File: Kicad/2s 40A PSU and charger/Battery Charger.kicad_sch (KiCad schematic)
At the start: 42 parts

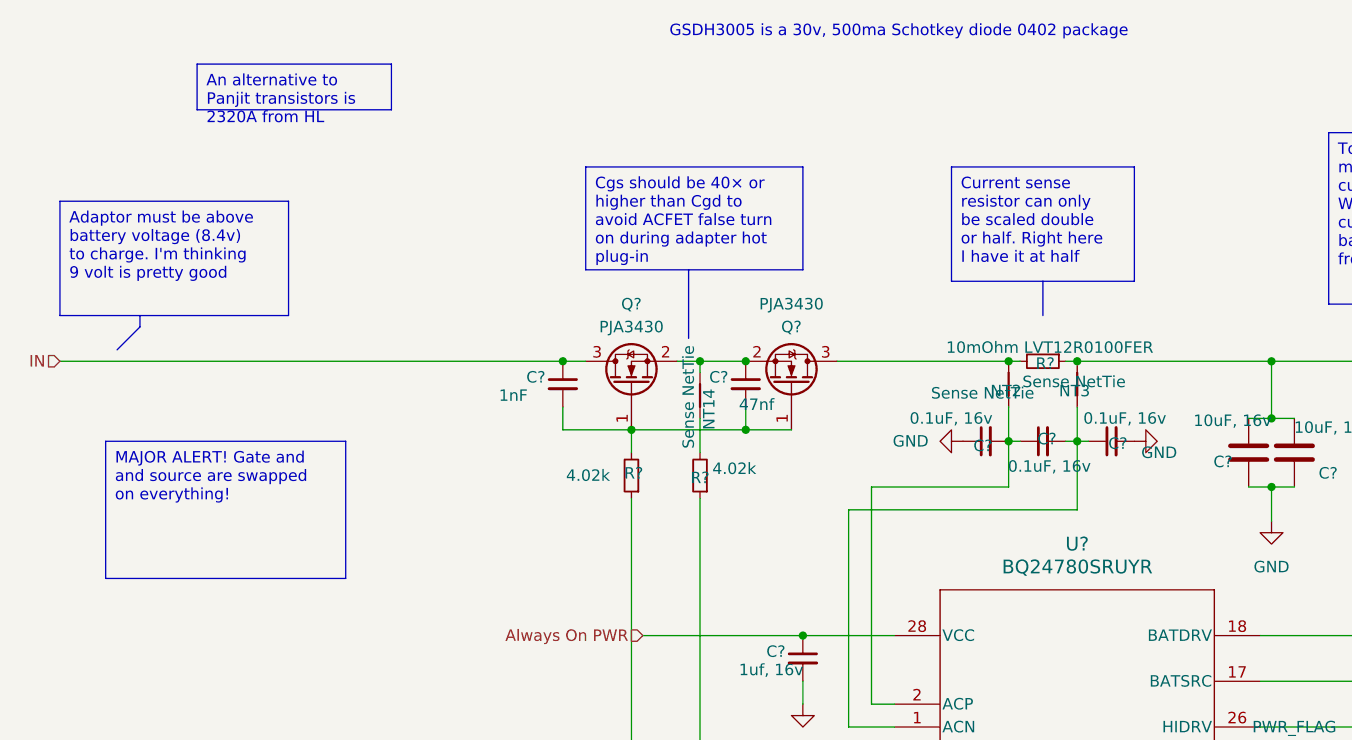
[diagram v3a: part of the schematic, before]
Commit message: Final tweaks, capacitor placement and GND keepouts
I tried my best to isolate signal grounds from the power paths. I also added a bunch of ground keepouts to help isolate.
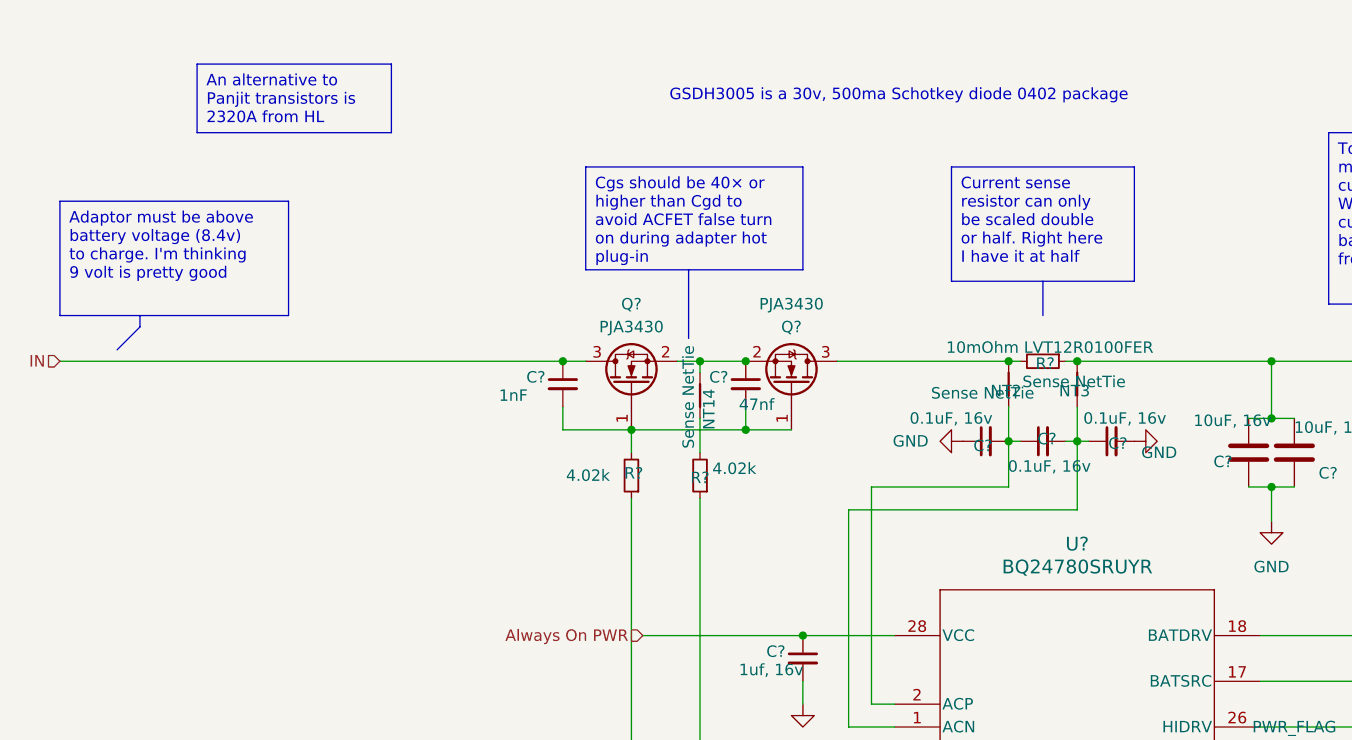
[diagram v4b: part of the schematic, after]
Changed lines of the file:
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@@
 	(title_block
 		(title "CACKLE 2s 40A PSU & Charger")
-		(date "2024-12-01")
+		(date "2024-12-23")
 		(rev "V1")
 		(comment 1 "Author: Asher Edwards")
@@
 		)
 	)
-	(text_box "MAJOR ALERT! Gate and and source are swapped on everything!"
+	(text_box "REGN is a 6v 100ma/13ma output"
 		(exclude_from_sim no)
-		(at 24.13 63.5 0)
-		(size 26.67 15.24)
+		(at 176.53 148.59 0)
+		(size 12.7 10.16)
 		(stroke
 			(width 0)
@@
 		)
 	)
-	(text_box "REGN is a 6v 100ma/13ma output"
+	(text_box "An alternative to Panjit transistors is 2320A from HL"
 		(exclude_from_sim no)
-		(at 176.53 148.59 0)
-		(size 12.7 10.16)
+		(at 34.29 21.59 0)
+		(size 21.59 7.62)
 		(stroke
 			(width 0)
@@
 		)
 	)
-	(text_box "An alternative to Panjit transistors is 2320A from HL"
+	(text_box "- ProcHot indicates system limit failure\n- PMON is total system power scaled down, so it needs an ext res\n- IDAP and IDCHG indicates adaptor and discharge current w/ Voltage\n- Acok is adaptor present indicator\n- TB_Stat indicated hybrid boost mode\n\nILIM and ACOK should not be left floating "
 		(exclude_from_sim no)
-		(at 34.29 21.59 0)
-		(size 21.59 5.08)
+		(at 25.4 123.19 0)
+		(size 36.83 33.02)
 		(stroke
 			(width 0)
@@
 		)
 	)
-	(text_box "- ProcHot indicates system limit failure\n- PMON is total system power scaled down, so it needs an ext res\n- IDAP and IDCHG indicates adaptor and discharge current w/ Voltage\n- Acok is adaptor present indicator\n- TB_Stat indicated hybrid boost mode\n\nILIM and ACOK should not be left floating "
+	(text "GSDH3005 is a 30v, 500ma Schotkey diode 0402 package"
 		(exclude_from_sim no)
-		(at 25.4 123.19 0)
-		(size 36.83 33.02)
-		(stroke
-			(width 0)
-			(type default)
-		)
-		(fill
-			(type none)
-		)
+		(at 112.268 25.146 0)
 		(effects
 			(font
-				(size 1.27 1.27)
-			)
-			(justify left top)
-		)
-	)
-	(text "GSDH3005 is a 30v, 500ma Schotkey diode 0402 package"
-		(exclude_from_sim no)
-		(at 112.268 18.034 0)
-		(effects
-			(font

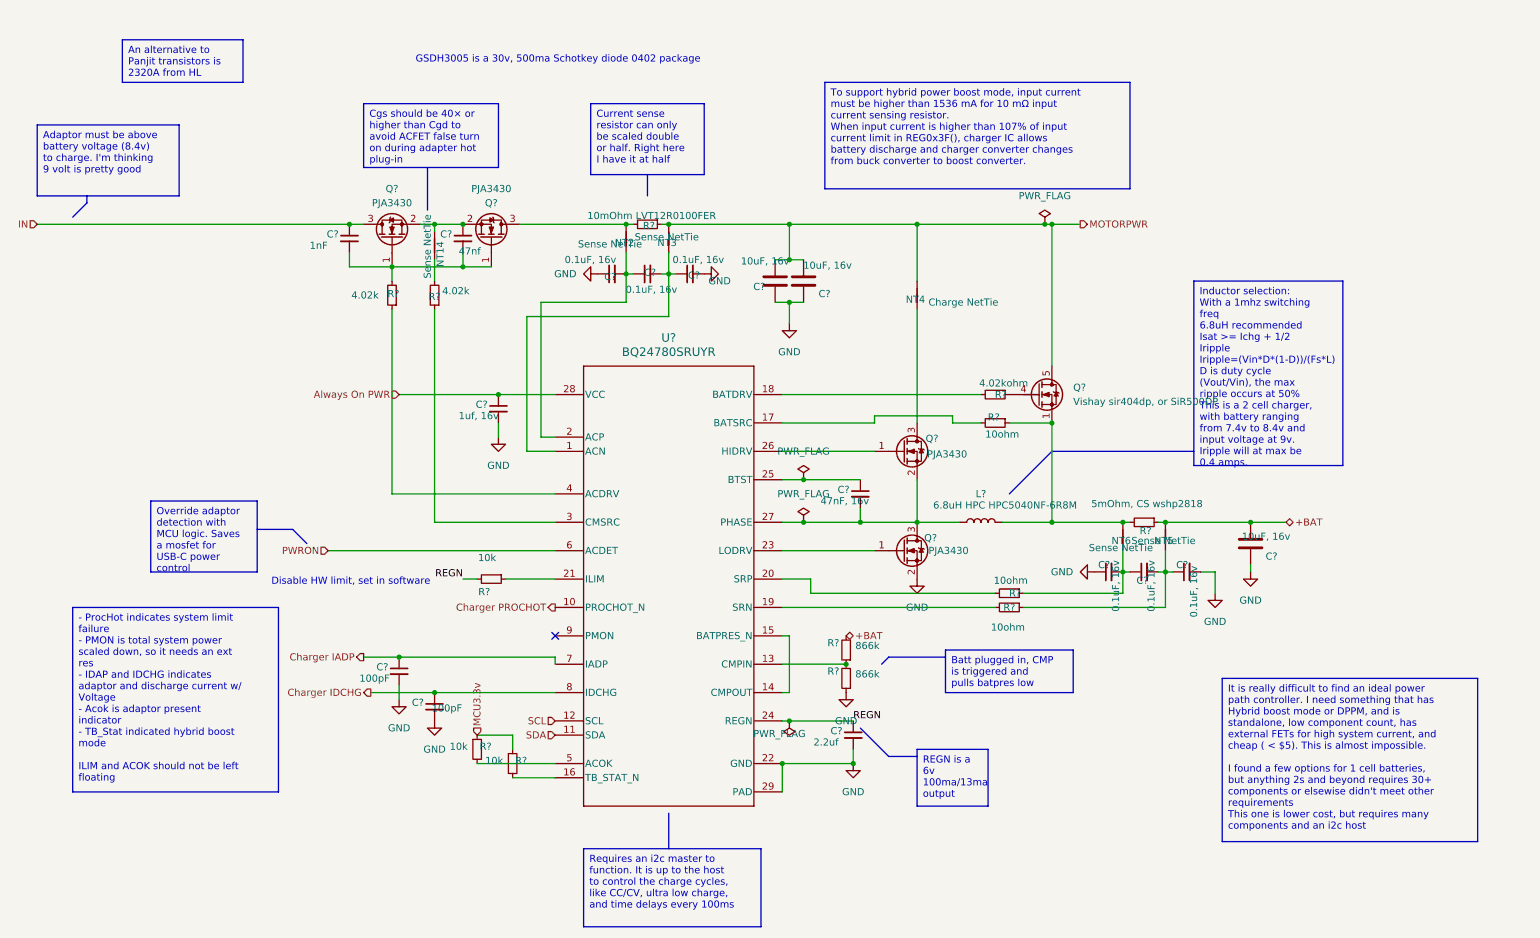
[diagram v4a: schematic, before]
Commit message: Added LCSC part numbers, DNP attr, and exported Gerbers
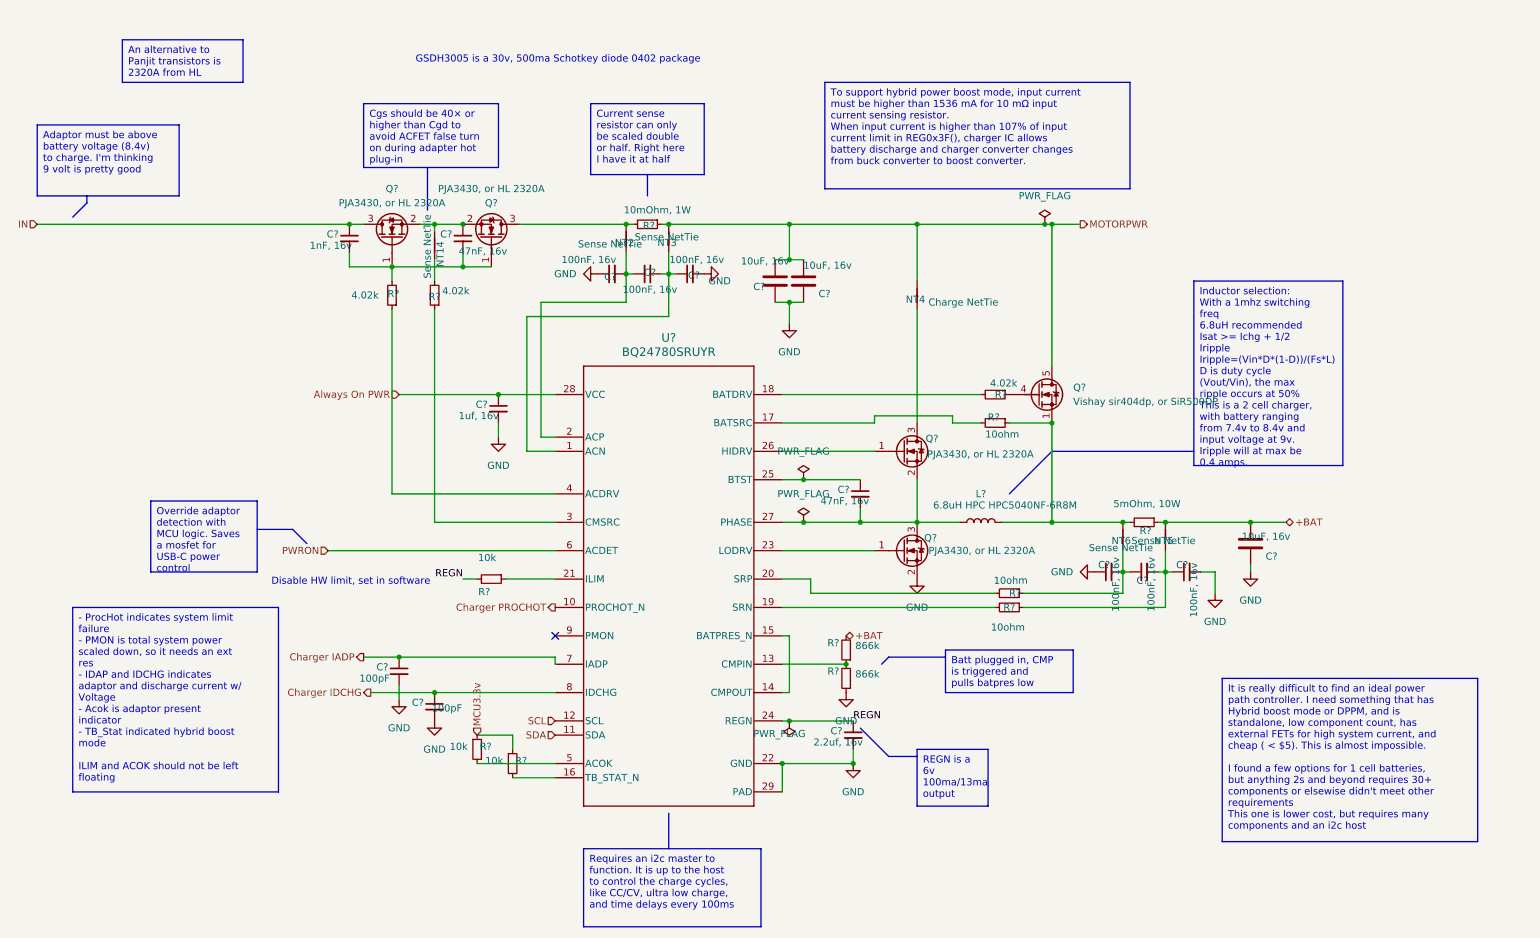
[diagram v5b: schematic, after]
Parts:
- C?: value 47nf -> 47nF, 16v
- C? (x6): value 0.1uF, 16v -> 100nF, 16v
- C?: value 1nF -> 1nF, 16v
- C?: value 2.2uf -> 2.2uf, 16v
- Q? (x4): value PJA3430 -> PJA3430, or HL 2320A
- R?: value 5mOhm, CS wshp2818 -> 5mOhm, 10W
- R?: value 4.02kohm -> 4.02k
- R?: value 10mOhm LVT12R0100FER -> 10mOhm, 1W
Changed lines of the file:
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@@
 			)
 		)
-		(property "Value" "PJA3430"
+		(property "Value" "PJA3430, or HL 2320A"
 			(at 178.562 113.03 0)
 			(effects
@@
 			)
 		)
-		(property "Value" "47nf"
+		(property "Value" "47nF, 16v"
 			(at 94.488 59.436 0)
 			(effects
@@
 			)
 		)
-		(property "Value" "5mOhm, CS wshp2818"
+		(property "Value" "5mOhm, 10W"
 			(at 217.678 104.648 90)
 			(effects
@@
 			)
 		)
-		(property "Value" "0.1uF, 16v"
+		(property "Value" "100nF, 16v"
 			(at 226.06 124.968 0)
 			(effects
@@
 			)
 		)
-		(property "Value" "0.1uF, 16v"
+		(property "Value" "100nF, 16v"
 			(at 218.44 123.952 0)
 			(effects
@@
 			)
 		)
-		(property "Value" "0.1uF, 16v"
+		(property "Value" "100nF, 16v"
 			(at 133.604 66.294 90)
 			(effects
@@
 			)
 		)
-		(property "Value" "4.02kohm"
+		(property "Value" "4.02k"
 			(at 192.024 83.058 90)
 			(effects
@@
 			)
 		)
-		(property "Value" "0.1uF, 16v"
+		(property "Value" "100nF, 16v"
 			(at 141.986 60.96 90)
 			(effects
@@
 			)
 		)
-		(property "Value" "0.1uF, 16v"
+		(property "Value" "100nF, 16v"
 			(at 122.682 60.96 90)
 			(effects
@@
 			)
 		)
-		(property "Value" "10mOhm LVT12R0100FER"
-			(at 129.032 53.086 90)
+		(property "Value" "10mOhm, 1W"
+			(at 130.048 52.07 90)
 			(effects
 				(font
@@
 			)
 		)
-		(property "Value" "PJA3430"
+		(property "Value" "PJA3430, or HL 2320A"
 			(at 178.308 95.758 0)
 			(effects
@@
 			)
 		)
-		(property "Value" "PJA3430"
+		(property "Value" "PJA3430, or HL 2320A"
 			(at 100.33 48.26 90)
 			(effects
@@
 			)
 		)
-		(property "Value" "1nF"
+		(property "Value" "1nF, 16v"
 			(at 67.818 58.42 0)
 			(effects
@@
 			)
 		)
-		(property "Value" "PJA3430"
+		(property "Value" "PJA3430, or HL 2320A"
 			(at 82.55 50.8 90)
 			(effects
@@
 			)
 		)
-		(property "Value" "0.1uF, 16v"
+		(property "Value" "100nF, 16v"
 			(at 212.09 123.952 0)
 			(effects
@@
 			)
 		)
-		(property "Value" "2.2uf"
+		(property "Value" "2.2uf, 16v"
 			(at 157.988 147.32 0)
 			(effects

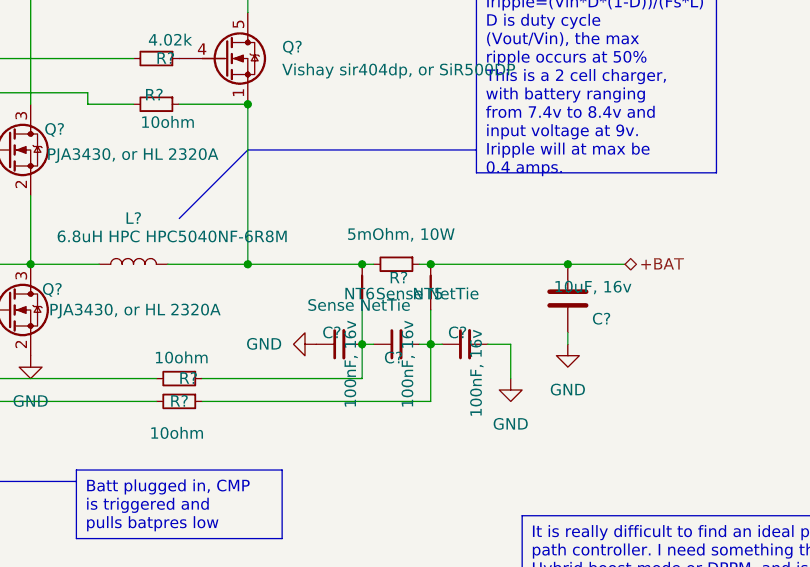
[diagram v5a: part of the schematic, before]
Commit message: Fixed Current sense resistor footprints, adjusted current GND blocks
I had to source alternative resistors and change the footprints as well. I didn't realize though that the 2818 footprint I had was wrong though, 2816 is not quite compatible!

Another thing I did was fix gnd guides and added horse shoe shapes around the sensitive component vias.
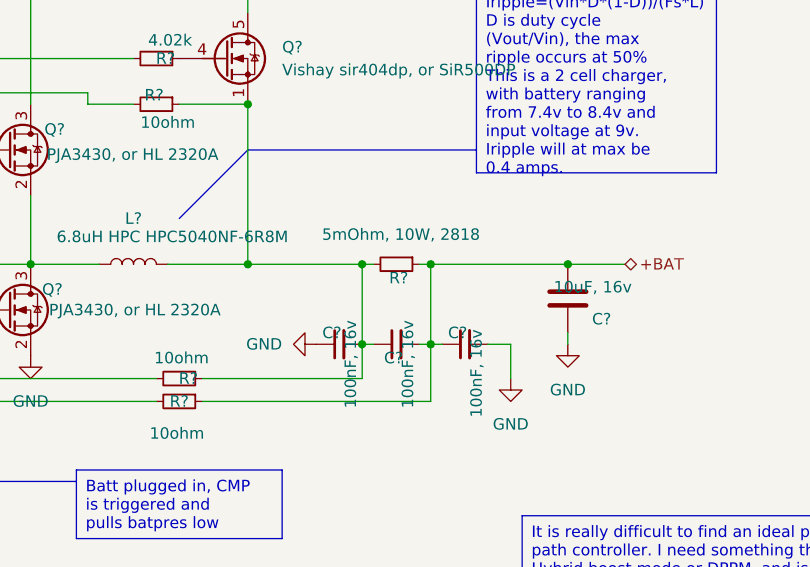
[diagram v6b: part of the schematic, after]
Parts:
- removed NT5, NT6: Sense NetTie, custom_Connector:NetTie-2_SMD_Pad0.2mm, symbol Device:NetTie_2
- R?: value 5mOhm, 10W -> 5mOhm, 10W, 2818; footprint Resistor_SMD:R_2816_7142Metric -> custom_Passives:R_Vishay_2818
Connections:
- net +BAT: now also C?.1, C?.2, R?.1
- net at C?.1, C?.2, R?.1: now also L?.2, Q?.1 (S), Q?.2 (S), Q?.3 (S), R?.1, R?.2
